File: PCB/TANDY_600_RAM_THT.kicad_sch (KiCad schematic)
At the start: 5 parts, among them J1 DIN 41612 2x22 male right-ang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, U1 628128_SOP, U2 74HC08

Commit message: tht routing
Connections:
- net A15: now also U2.10; no longer U2.4
- net A16: now also U2.6, U2.9; no longer U2.3, U2.5
- net GND: now also U2.1, U2.2; no longer U2.10, U2.9
- net ~{CS1_A}: now also U2.4; no longer U2.2
- net ~{CS1_B}: now also U2.5; no longer U2.1
- net ~{CS1}: now also U2.8; no longer U2.6
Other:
- moved on the sheet: U2A, U2B, U2C
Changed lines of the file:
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@@
   (title_block
     (title "96K RAM for TANDY 600")
-    (date "2022-09-27")
-    (rev "010")
+    (date "2022-10-01")
+    (rev "011")
     (company "Brian K. White - b.kenyon.w@gmail.com")
     (comment 1 "LICENSE: CC-BY-SA 4.0")
@@
     (comment 3 "Replaces TANDY Cat. No. 26-3910 \"OPRM\"")
   )
+  (junction (at 125.73 102.87) (diameter 0) (color 0 0 0 0)
+  )
   (junction (at 140.97 109.22) (diameter 0) (color 0 0 0 0)
-  )
-  (junction (at 125.73 102.87) (diameter 0) (color 0 0 0 0)
   )
   (junction (at 140.97 96.52) (diameter 0) (color 0 0 0 0)
@@
     (pin "9")
   )
-  (symbol (lib_id "000_LOCAL:74HC08") (at 133.35 109.22 0) (mirror x) (unit 1)
-    (in_bom yes) (on_board yes)
-    (property "Reference" "U2" (id 0) (at 133.35 109.22 0))
-    (property "Value" "74HC08" (id 1) (at 133.35 115.57 0)
-      (effects (font (size 1.27 1.27)) hide)
-    )
-    (property "Footprint" "000_LOCAL:DIP-14_W7.62mm" (id 2) (at 133.35 109.22 0)
-      (effects (font (size 1.27 1.27)) hide)
-    )
-    (property "Datasheet" "https://assets.nexperia.com/documents/data-sheet/74HC_HCT08.pdf" (id 3) (at 133.35 109.22 0)
+  (symbol (lib_id "000_LOCAL:74HC08") (at 133.35 158.75 0) (mirror x) (unit 1)
+    (in_bom yes) (on_board yes)
+    (property "Reference" "U2" (id 0) (at 133.35 158.75 0))
+    (property "Value" "74HC08" (id 1) (at 133.35 165.1 0)
+      (effects (font (size 1.27 1.27)) hide)
+    )
+    (property "Footprint" "000_LOCAL:DIP-14_W7.62mm" (id 2) (at 133.35 158.75 0)
+      (effects (font (size 1.27 1.27)) hide)
+    )
+    (property "Datasheet" "https://assets.nexperia.com/documents/data-sheet/74HC_HCT08.pdf" (id 3) (at 133.35 158.75 0)
       (effects (font (size 1.27 1.27)) hide)
     )
@@
     (pin "7")
   )
-  (symbol (lib_id "000_LOCAL:74HC08") (at 133.35 158.75 0) (mirror x) (unit 3)
-    (in_bom yes) (on_board yes)
-    (property "Reference" "U2" (id 0) (at 133.35 158.75 0))
-    (property "Value" "74HC08" (id 1) (at 133.35 165.354 0)
-      (effects (font (size 1.27 1.27)) hide)
-    )
-    (property "Footprint" "000_LOCAL:DIP-14_W7.62mm" (id 2) (at 133.35 158.75 0)
-      (effects (font (size 1.27 1.27)) hide)
-    )
-    (property "Datasheet" "https://assets.nexperia.com/documents/data-sheet/74HC_HCT08.pdf" (id 3) (at 133.35 158.75 0)
+  (symbol (lib_id "000_LOCAL:74HC08") (at 148.59 102.87 0) (mirror x) (unit 3)
+    (in_bom yes) (on_board yes)
+    (property "Reference" "U2" (id 0) (at 148.59 102.87 0))
+    (property "Value" "74HC08" (id 1) (at 148.59 109.474 0)
+      (effects (font (size 1.27 1.27)) hide)
+    )
+    (property "Footprint" "000_LOCAL:DIP-14_W7.62mm" (id 2) (at 148.59 102.87 0)
+      (effects (font (size 1.27 1.27)) hide)
+    )
+    (property "Datasheet" "https://assets.nexperia.com/documents/data-sheet/74HC_HCT08.pdf" (id 3) (at 148.59 102.87 0)
       (effects (font (size 1.27 1.27)) hide)
     )
@@
     (pin "1")
   )
-  (symbol (lib_id "000_LOCAL:74HC08") (at 148.59 102.87 0) (unit 2)
-    (in_bom yes) (on_board yes)
-    (property "Reference" "U2" (id 0) (at 148.59 102.87 0))
-    (property "Value" "74HC08" (id 1) (at 148.59 96.52 0)
-      (effects (font (size 1.27 1.27)) hide)
-    )
-    (property "Footprint" "000_LOCAL:DIP-14_W7.62mm" (id 2) (at 148.59 102.87 0)
-      (effects (font (size 1.27 1.27)) hide)
-    )
-    (property "Datasheet" "https://assets.nexperia.com/documents/data-sheet/74HC_HCT08.pdf" (id 3) (at 148.59 102.87 0)
-      (effects (font (size 1.27 1.27)) hide)
-    )
+  (symbol (lib_id "000_LOCAL:74HC08") (at 133.35 109.22 0) (unit 2)
+    (in_bom yes) (on_board yes)
+    (property "Reference" "U2" (id 0) (at 133.35 109.22 0))
+    (property "Value" "74HC08" (id 1) (at 133.35 102.87 0)
+      (effects (font (size 1.27 1.27)) hide)
+    )
+    (property "Footprint" "000_LOCAL:DIP-14_W7.62mm" (id 2) (at 133.35 109.22 0)
+      (effects (font (size 1.27 1.27)) hide)
+    )
+    (property "Datasheet" "https://assets.nexperia.com/documents/data-sheet/74HC_HCT08.pdf" (id 3) (at 133.35 109.22 0)
+      (effects (font (size 1.27 1.27)) hide)
+    )

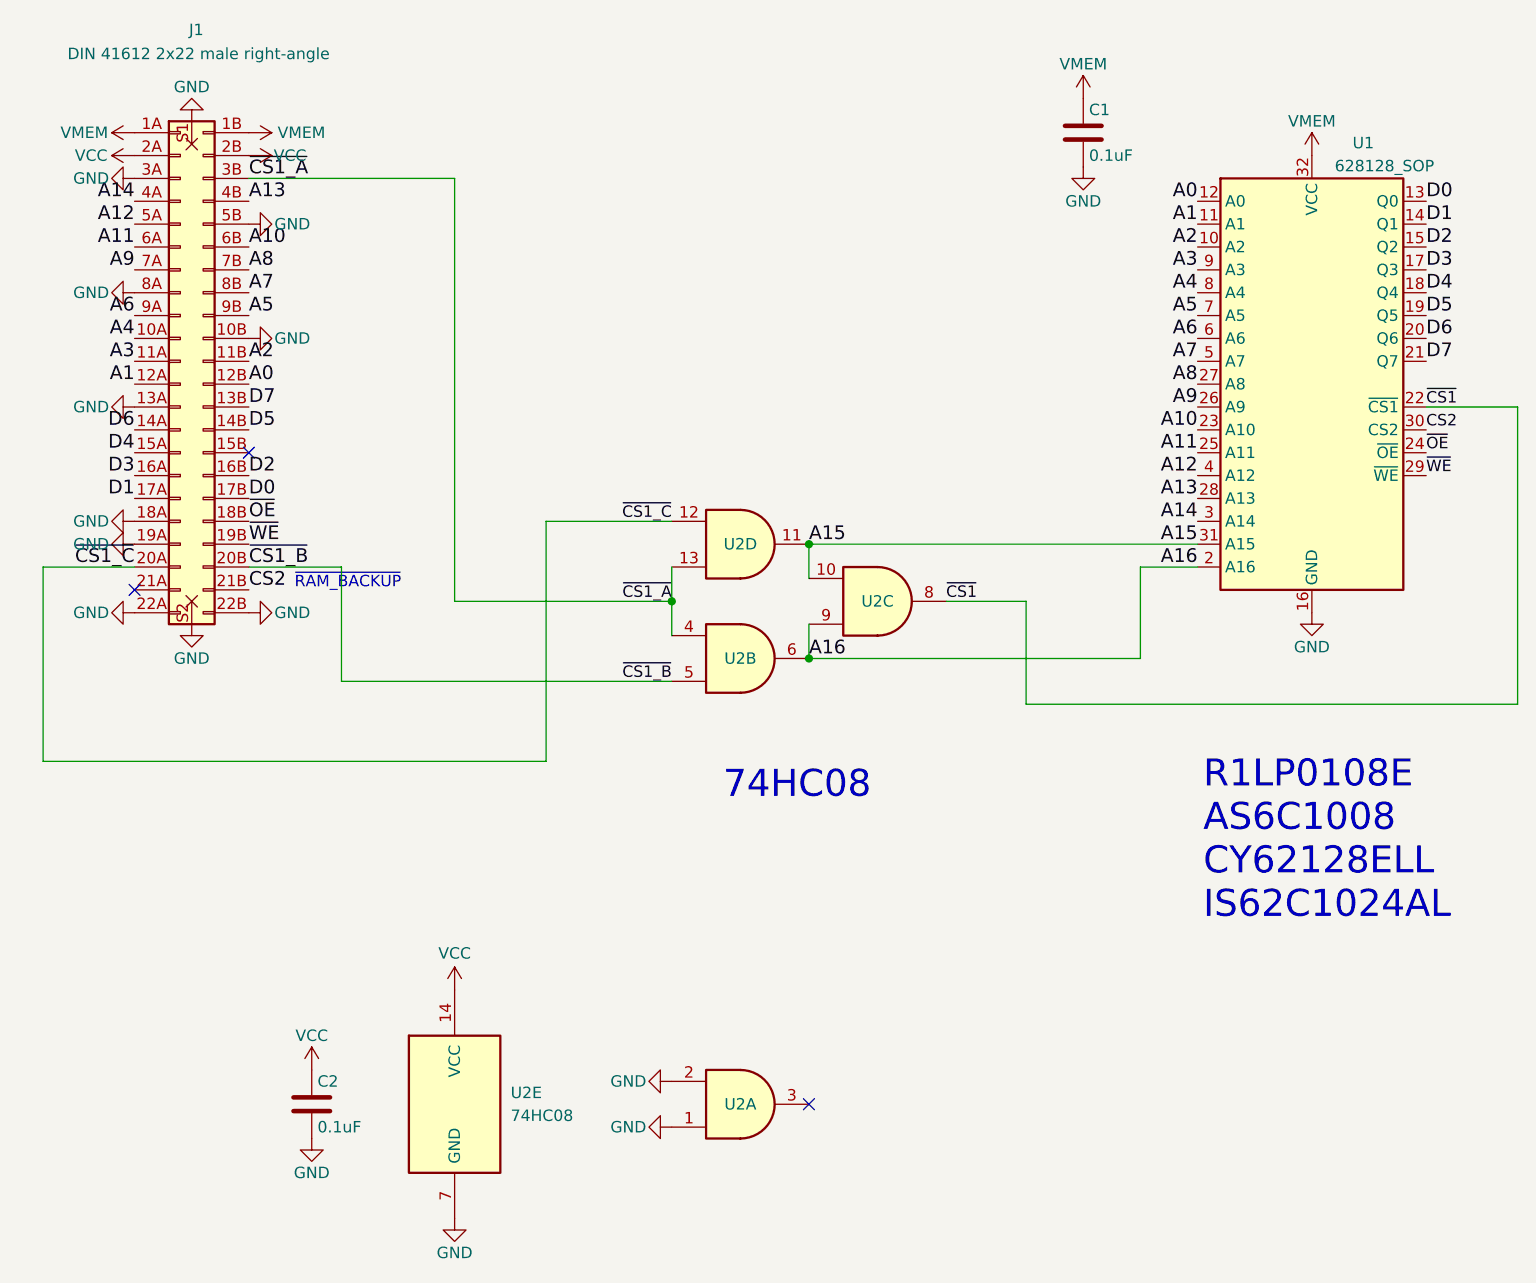
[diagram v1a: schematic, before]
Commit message: gnd on tiny, new dual sch, bus connector symbol & footprint
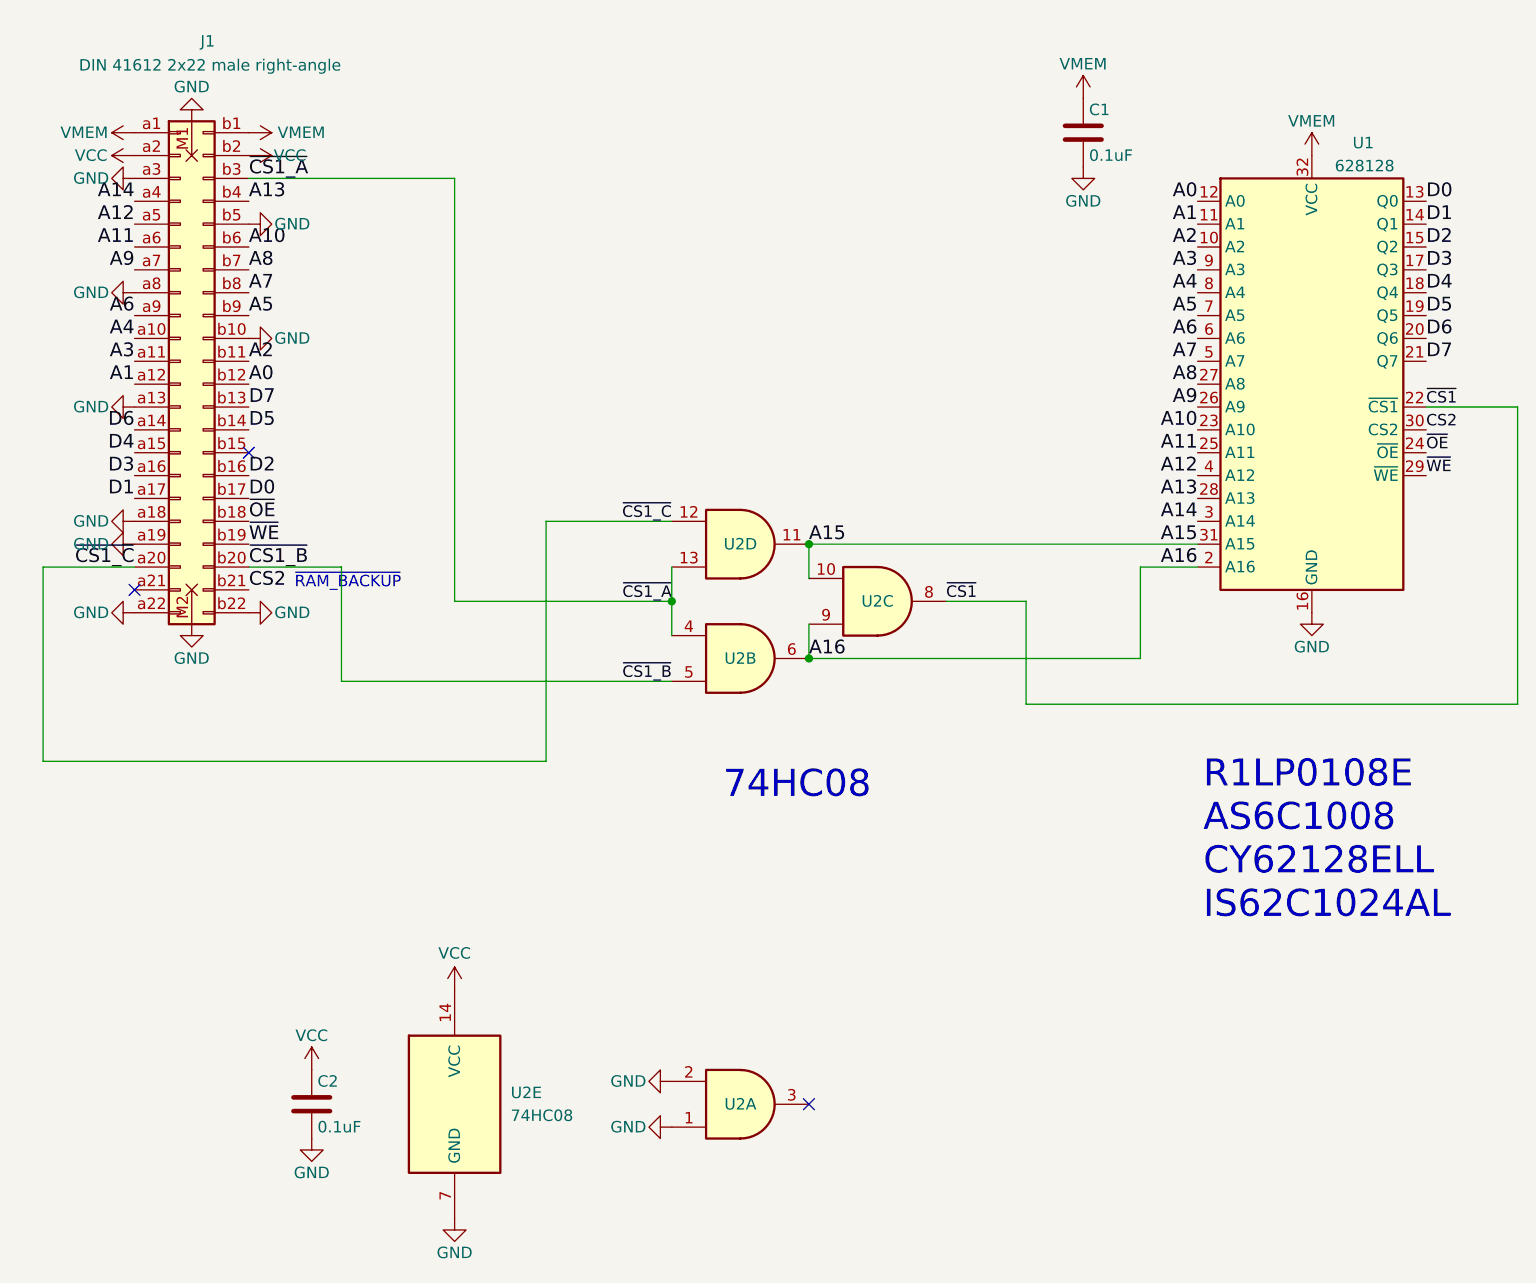
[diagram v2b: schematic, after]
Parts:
- U1: value 628128_SOP -> 628128
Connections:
- net A0: now also J1.b12; no longer J1.12B
- net A1: now also J1.a12; no longer J1.12A
- net A10: now also J1.b6; no longer J1.6B
- net A11: now also J1.a6; no longer J1.6A
- net A12: now also J1.a5; no longer J1.5A
- net A13: now also J1.b4; no longer J1.4B
- net A14: now also J1.a4; no longer J1.4A
- net A2: now also J1.b11; no longer J1.11B
- net A3: now also J1.a11; no longer J1.11A
- net A4: now also J1.a10; no longer J1.10A
- net A5: now also J1.b9; no longer J1.9B
- net A6: now also J1.a9; no longer J1.9A
- net A7: now also J1.b8; no longer J1.8B
- net A8: now also J1.b7; no longer J1.7B
- net A9: now also J1.a7; no longer J1.7A
- net CS2: now also J1.b21; no longer J1.21B
- net D0: now also J1.b17; no longer J1.17B
- net D1: now also J1.a17; no longer J1.17A
- net D2: now also J1.b16; no longer J1.16B
- net D3: now also J1.a16; no longer J1.16A
- net D4: now also J1.a15; no longer J1.15A
- net D5: now also J1.b14; no longer J1.14B
- net D6: now also J1.a14; no longer J1.14A
- net D7: now also J1.b13; no longer J1.13B
- net GND: now also J1.M1 (mount), J1.M2 (mount), J1.a13, J1.a18, J1.a19, J1.a22, J1.a3, J1.a8, J1.b10, J1.b22, J1.b5; no longer J1.10B, J1.13A, J1.18A, J1.19A, J1.22A, J1.22B, J1.3A, J1.5B, J1.8A, J1.S1 (mount), J1.S2 (mount)
- net VCC: now also J1.a2, J1.b2; no longer J1.2A, J1.2B
- net VMEM: now also J1.a1, J1.b1; no longer J1.1A, J1.1B
- net ~{CS1_A}: now also J1.b3; no longer J1.3B
- net ~{CS1_B}: now also J1.b20; no longer J1.20B
- net ~{CS1_C}: now also J1.a20; no longer J1.20A
- net ~{OE}: now also J1.b18; no longer J1.18B
- net ~{WE}: now also J1.b19; no longer J1.19B
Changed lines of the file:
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@@
   (title_block
     (title "96K RAM for TANDY 600")
-    (date "2022-10-01")
-    (rev "011")
+    (date "2022-10-04")
+    (rev "THT_012")
     (company "Brian K. White - b.kenyon.w@gmail.com")
     (comment 1 "LICENSE: CC-BY-SA 4.0")
@@
     (pin "2")
   )
-  (symbol (lib_id "000_LOCAL:DIN 41612 2x22 male right-angle") (at 71.12 76.2 0) (unit 1)
-    (in_bom yes) (on_board yes)
-    (property "Reference" "J1" (id 0) (at 72.898 39.37 0))
-    (property "Value" "DIN 41612 2x22 male right-angle" (id 1) (at 73.152 42.037 0))
-    (property "Footprint" "000_LOCAL:DIN 41612 2x22 male right-angle" (id 2) (at 71.12 76.2 0)
-      (effects (font (size 1.27 1.27)) hide)
-    )
-    (property "Datasheet" "~" (id 3) (at 71.12 76.2 0)
-      (effects (font (size 1.27 1.27)) hide)
-    )
-    (pin "10A")
-    (pin "10B")
-    (pin "11A")
-    (pin "11B")
-    (pin "12A")
-    (pin "12B")
-    (pin "13A")
-    (pin "13B")
-    (pin "14A")
-    (pin "14B")
-    (pin "15A")
-    (pin "15B")
-    (pin "16A")
-    (pin "16B")
-    (pin "17A")
-    (pin "17B")
-    (pin "18A")
-    (pin "18B")
-    (pin "19A")
-    (pin "19B")
-    (pin "1A")
-    (pin "1B")
-    (pin "20A")
-    (pin "20B")
-    (pin "21A")
-    (pin "21B")
-    (pin "22A")
-    (pin "22B")
-    (pin "2A")
-    (pin "2B")
-    (pin "3A")
-    (pin "3B")
-    (pin "4A")
-    (pin "4B")
-    (pin "5A")
-    (pin "5B")
-    (pin "6A")
-    (pin "6B")
-    (pin "7A")
-    (pin "7B")
-    (pin "8A")
-    (pin "8B")
-    (pin "9A")
-    (pin "9B")
-    (pin "S1")
-    (pin "S2")
+  (symbol (lib_id "000_LOCAL:DIN 41612 2x22 male right-angle") (at 72.39 77.47 0) (unit 1)
+    (in_bom yes) (on_board yes)
+    (property "Reference" "J1" (id 0) (at 74.168 40.64 0))
+    (property "Value" "DIN 41612 2x22 male right-angle" (id 1) (at 74.422 43.307 0))
+    (property "Footprint" "000_LOCAL:DIN 41612 2x22 male right-angle" (id 2) (at 72.39 77.47 0)
+      (effects (font (size 1.27 1.27)) hide)
+    )
+    (property "Datasheet" "~" (id 3) (at 72.39 77.47 0)
+      (effects (font (size 1.27 1.27)) hide)
+    )
+    (pin "M1")
+    (pin "M2")
+    (pin "a1")
+    (pin "a10")
+    (pin "a11")
+    (pin "a12")
+    (pin "a13")
+    (pin "a14")
+    (pin "a15")
+    (pin "a16")
+    (pin "a17")
+    (pin "a18")
+    (pin "a19")
+    (pin "a2")
+    (pin "a20")
+    (pin "a21")
+    (pin "a22")
+    (pin "a3")
+    (pin "a4")
+    (pin "a5")
+    (pin "a6")
+    (pin "a7")
+    (pin "a8")
+    (pin "a9")
+    (pin "b1")
+    (pin "b10")
+    (pin "b11")
+    (pin "b12")
+    (pin "b13")
+    (pin "b14")
+    (pin "b15")
+    (pin "b16")
+    (pin "b17")
+    (pin "b18")
+    (pin "b19")
+    (pin "b2")
+    (pin "b20")
+    (pin "b21")
+    (pin "b22")
+    (pin "b3")
+    (pin "b4")
+    (pin "b5")
+    (pin "b6")
+    (pin "b7")
+    (pin "b8")
+    (pin "b9")
   )
   (symbol (lib_id "000_LOCAL:VMEM") (at 66.04 50.8 90) (unit 1)
@@
     (in_bom yes) (on_board yes)
     (property "Reference" "U1" (id 0) (at 202.565 51.943 0))
-    (property "Value" "628128_SOP" (id 1) (at 199.39 55.245 0)
+    (property "Value" "628128" (id 1) (at 199.39 55.245 0)
       (effects (font (size 1.27 1.27)) (justify left bottom))
     )
@@
     )
     (path "/00000000-0000-0000-0000-0000613c8a04"
-      (reference "U1") (unit 1) (value "628128_SOP") (footprint "000_LOCAL:DIP-32_W15.24mm")
+      (reference "U1") (unit 1) (value "628128") (footprint "000_LOCAL:DIP-32_W15.24mm")
     )
     (path "/044f6254-2d63-4897-a62f-222c3e6a86ff"

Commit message: add full-size dual
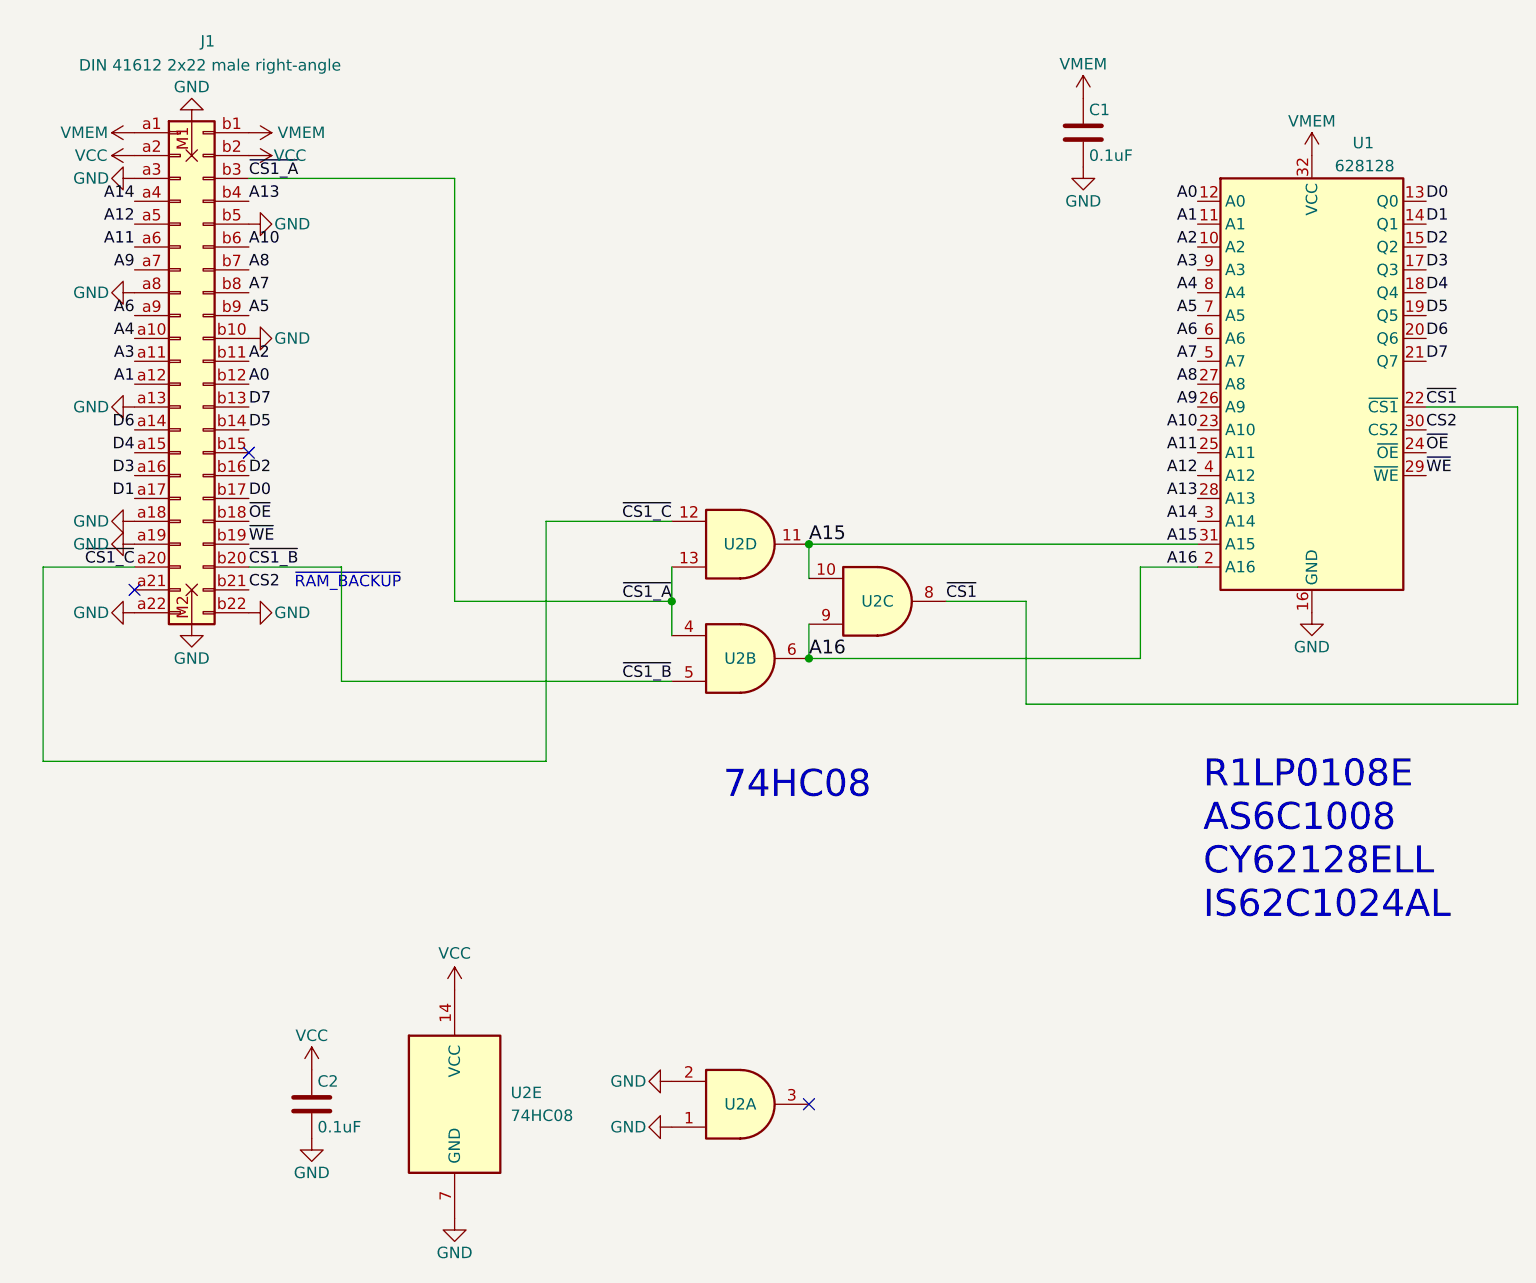
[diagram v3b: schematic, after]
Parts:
- J1: symbol 000_LOCAL:DIN 41612 2x22 male right-angle -> 000_LOCAL:DIN_41612_02x22

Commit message: footprints, ground paths
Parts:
- J1: footprint 000_LOCAL:DIN 41612 2x22 male right-angle -> 000_LOCAL:DIN-41612_02x22_male_horizontal
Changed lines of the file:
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@@
     (property "Reference" "J1" (id 0) (at 74.168 40.64 0))
     (property "Value" "DIN 41612 2x22 male right-angle" (id 1) (at 74.422 43.307 0))
-    (property "Footprint" "000_LOCAL:DIN 41612 2x22 male right-angle" (id 2) (at 71.12 76.2 0)
+    (property "Footprint" "000_LOCAL:DIN-41612_02x22_male_horizontal" (id 2) (at 71.12 76.2 0)
       (effects (font (size 1.27 1.27)) hide)
     )
@@
     )
     (path "/00000000-0000-0000-0000-000061163f2f"
-      (reference "J1") (unit 1) (value "DIN 41612 2x22 male right-angle") (footprint "000_LOCAL:DIN 41612 2x22 male right-angle")
+      (reference "J1") (unit 1) (value "DIN 41612 2x22 male right-angle") (footprint "000_LOCAL:DIN-41612_02x22_male_horizontal")
     )
     (path "/00000000-0000-0000-0000-0000613c8a04"
